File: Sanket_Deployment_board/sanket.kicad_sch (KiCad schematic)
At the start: 38 parts, among them J1 Conn_01x03, J2 Conn_02x03_Counter_Clockwise, J3 Conn_02x03_Counter_Clockwise, J4 Conn_01x01_Socket, J7 Conn_01x01_Socket, J8 Conn_01x05, Q1 NMOS, Q2 NMOS, U2 SN74LVC1G17QDCKRQ1, U3 TPS5420D, U4 74AHC1G00

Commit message: Routing done, 1st review to be done
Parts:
- removed J7: Conn_01x01_Socket, Connector_PinSocket_2.54mm:PinSocket_1x01_P2.54mm_Vertical, symbol Connector:Conn_01x01_Socket
- removed Q1, Q2: NMOS, NMOS_sanket:LFPAK56_SOT669_NEX-M, symbol Simulation_SPICE:NMOS
- removed TP3, TP4: TestPoint, TestPoint:TestPoint_THTPad_1.0x1.0mm_Drill0.5mm, symbol Connector:TestPoint
- removed U4: 74AHC1G00, NAND_sanket:DCK5_TEX-L, symbol 74xGxx:74AHC1G00
- added MOSFET1, MOSFET2: BUK9Y21-40E_115, NMOS_sanket:LFPAK56_SOT669_NEX-M, symbol NMOS_ADS:BUK9Y21-40E_115
- added U1: SN74LV1T00DCKR, NAND_sanket:DCK5_TEX-L, symbol NAND_ADS:SN74LV1T00DCKR
- C1: value 2u2 -> (none)
- C10: value 4.7u -> (none)
- C2, C8: value 100n -> (none)
- C3: value 10n -> (none)
- C4, C5: value 47u -> (none)
- C6: value 150p -> (none)
- C9: value 1800p -> (none)
- D1: value D -> (none); footprint Wurth inductor:DIOM7959X261N -> Diode_in_TP5420:CR_MBRS340_ONS-M
- H1, H2, H3, H4: value MountingHole -> (none)
- J1: value Conn_01x03 -> (none)
- J4: value Conn_01x01_Socket -> (none)
- J8: value Conn_01x05 -> (none)
- L1: value 18u -> (none)
- R1: value 1k -> (none)
- R2, R3, R4: value 100k -> (none)
- R5: value 1M -> (none)
- R6: value 549 -> (none)
- R7: value 5.9K -> (none)
- R8: value 10k -> (none)
- TP1, TP2: value TestPoint -> (none)
- U2: value SN74LVC1G17QDCKRQ1 -> (none); footprint Package_TO_SOT_SMD:SOT-353_SC-70-5 -> Schmitt_trigger_ADS:DCK5-M
- U3: value TPS5420D -> (none); footprint Package_SO:SOIC-8_3.9x4.9mm_P1.27mm -> TPS5420:D8-M
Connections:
- net 3V3: now also J2.6 (Pin_6), U1.5 (VCC); no longer J2.1 (Pin_1)
- net ARM: now also MOSFET1.4
- net BurnWire1IN: now also J2.1 (Pin_1); no longer J2.4 (Pin_4)
- net BurnWire1OUT: now also J2.2 (Pin_2), J2.4 (Pin_4), J3.1 (Pin_1); no longer J2.5 (Pin_5), J2.6 (Pin_6), J3.4 (Pin_4)
- net DEPLOY: now also U1.4 (Y)
- net DeployerDetectionSW1OUT: now also J2.5 (Pin_5), J3.6 (Pin_6); no longer J2.2 (Pin_2), J3.1 (Pin_1)
- net DeployerDetectionSW2OUT: now also J3.5 (Pin_5); no longer J3.2 (Pin_2)
- net FIRE: now also MOSFET2.4, U1.2 (B)
- net GND: now also MOSFET2.1, MOSFET2.2, MOSFET2.3, U1.3 (GND); no longer J3.5 (Pin_5), J3.6 (Pin_6)
- net TriggerOUT: now also U1.1 (A)
- new net: MOSFET1.1, MOSFET1.2, MOSFET1.3, MOSFET2.5
- new net NMOS_DRAIN: J3.2 (Pin_2), J3.4 (Pin_4), MOSFET1.5
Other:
- moved on the sheet: J2, R3, R4

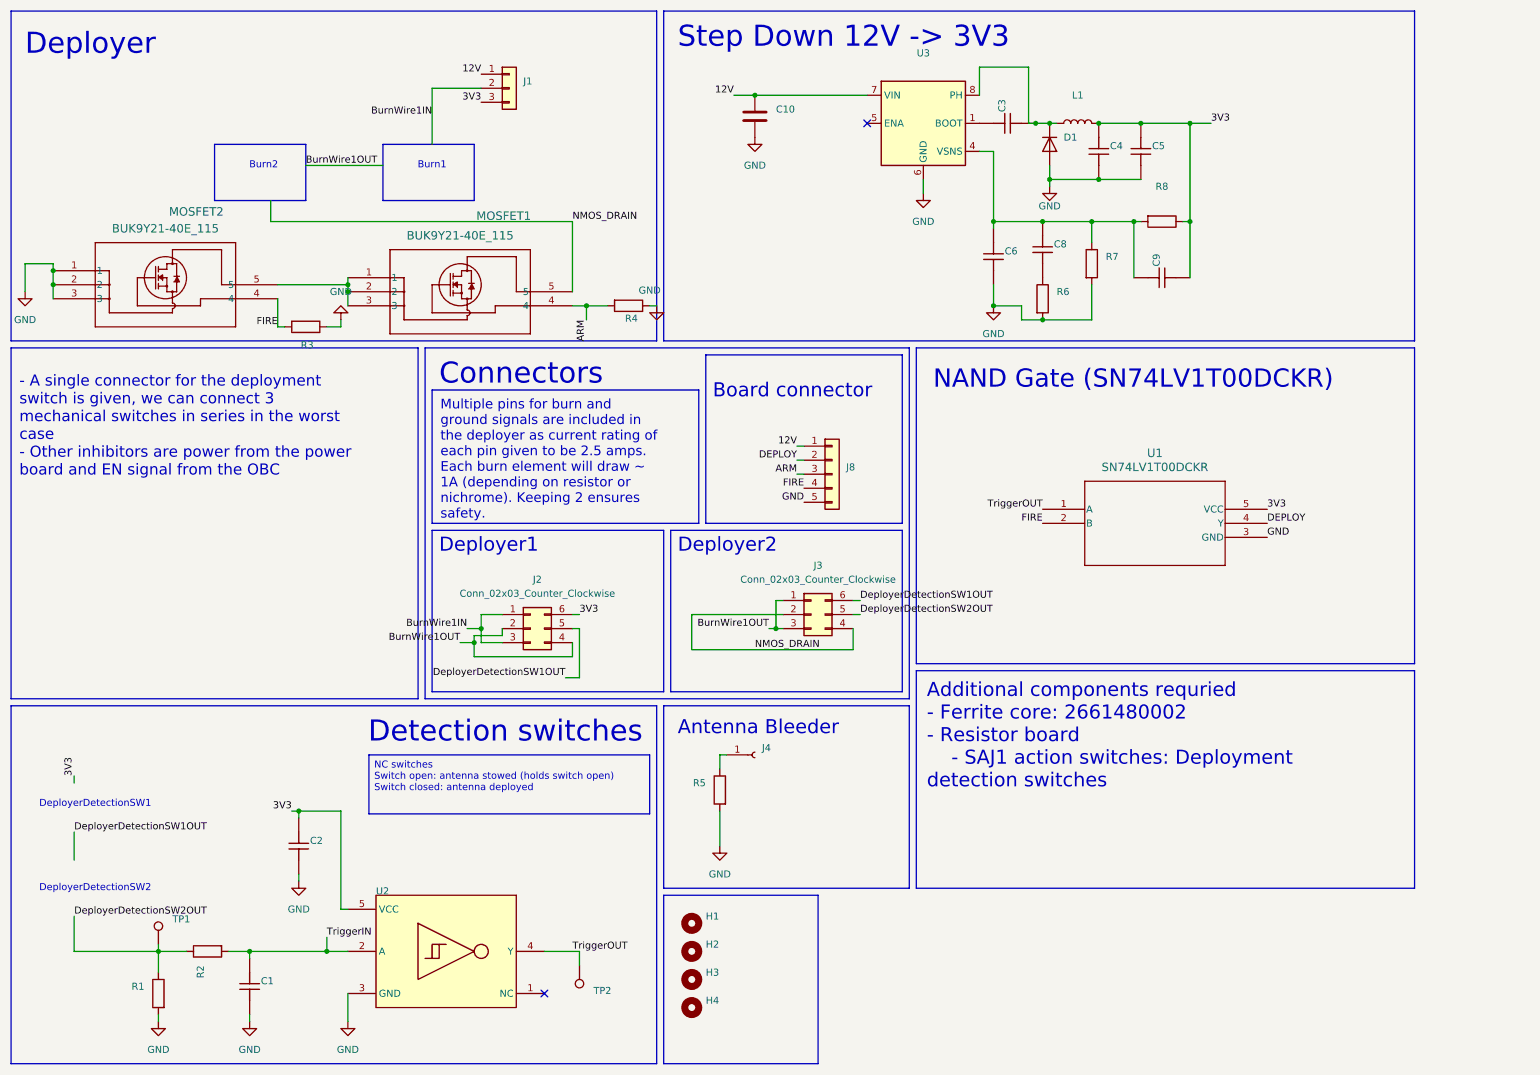
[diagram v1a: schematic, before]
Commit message: Added missing holw in resistor board, removed NAND gate, added more testpoints
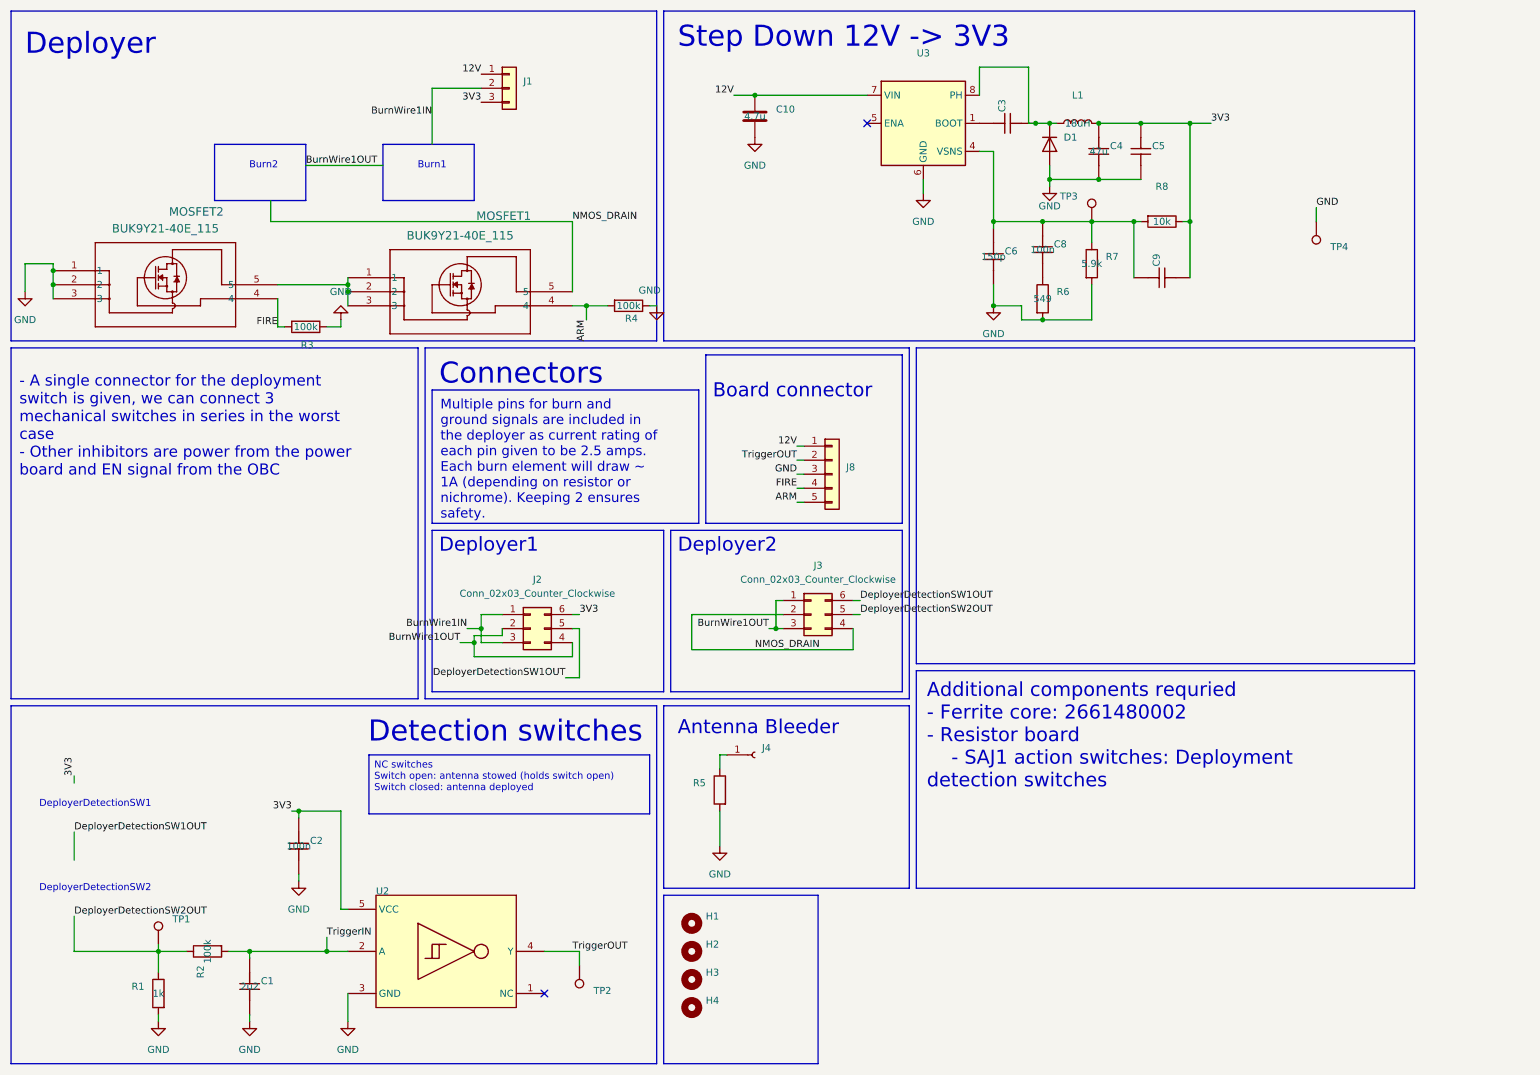
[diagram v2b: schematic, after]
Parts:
- removed U1: SN74LV1T00DCKR, NAND_sanket:DCK5_TEX-L, symbol NAND_ADS:SN74LV1T00DCKR
- added TP3, TP4: (no value), TestPoint:TestPoint_THTPad_1.0x1.0mm_Drill0.5mm, symbol Connector:TestPoint
- C1: value (none) -> 2u2
- C10: value (none) -> 4.7u
- C2, C8: value (none) -> 100n
- C4, C5: value (none) -> 47u
- C6: value (none) -> 150p
- L1: value (none) -> 18uH
- R1: value (none) -> 1k
- R2, R3, R4: value (none) -> 100k
- R6: value (none) -> 549
- R7: value (none) -> 5.9k
- R8: value (none) -> 10k
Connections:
- net DEPLOY is gone; now on net TriggerOUT: J8.2 (Pin_2)
- net ARM: now also J8.5 (Pin_5); no longer J8.3 (Pin_3)
- net GND: now also J8.3 (Pin_3), TP4.1; no longer J8.5 (Pin_5)
- net at C6.2, C8.2, C9.2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: now also TP3.1
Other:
- note removed: "NAND Gate (SN74LV1T00DCKR)"

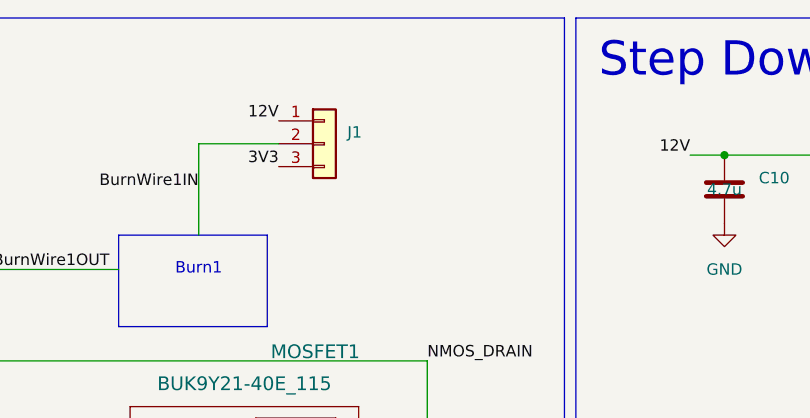
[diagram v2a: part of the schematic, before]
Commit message: Added extra pads for sized resistors
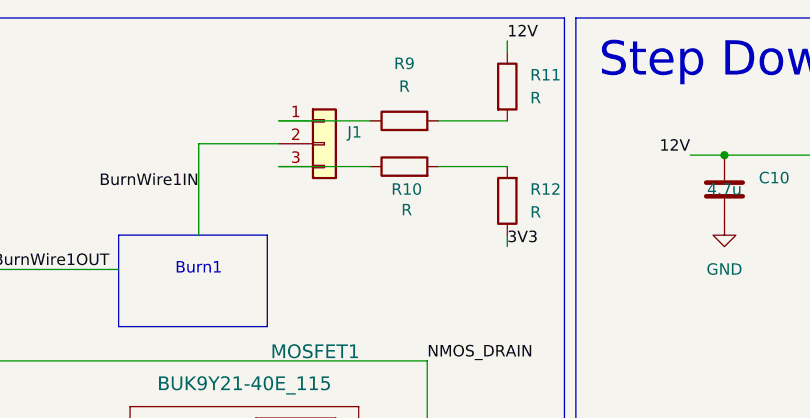
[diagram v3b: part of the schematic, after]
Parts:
- added R10, R11, R12, R9: R, Resistor_SMD:R_0805_2012Metric, symbol Device:R
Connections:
- net 12V: now also R11.1; no longer J1.1 (Pin_1)
- net 3V3: now also R12.1; no longer J1.3 (Pin_3)
- new net: R10.2, R12.2
- new net: J1.3 (Pin_3), R10.1
- new net: J1.1 (Pin_1), R9.1
- new net: R11.2, R9.2

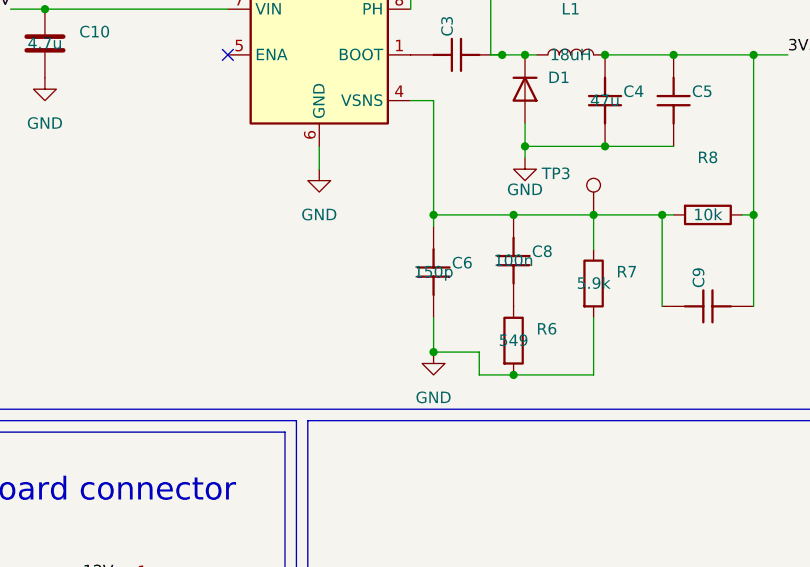
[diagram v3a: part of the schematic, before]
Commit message: Resistor board for nichrome added
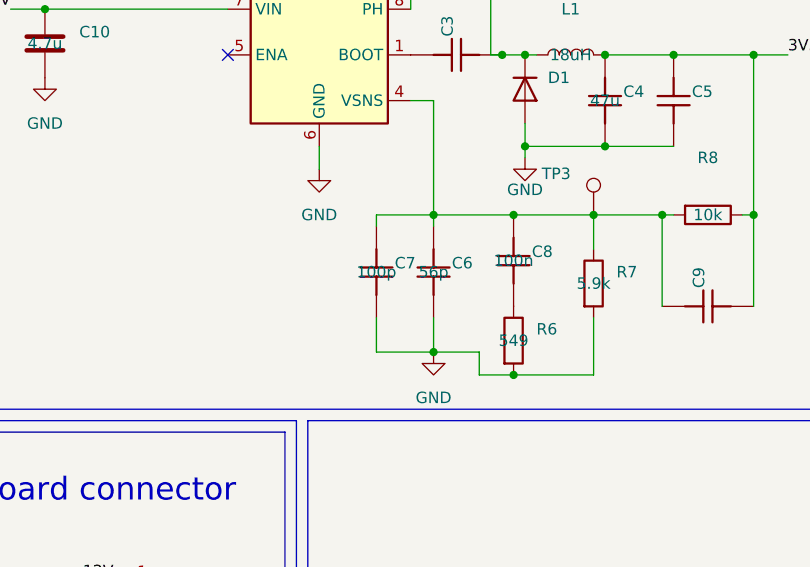
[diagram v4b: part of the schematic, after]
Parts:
- added C7: 100p, Capacitor_SMD:C_0805_2012Metric, symbol sanket 4.0-altium-import:root_1_CAP-CER-0.1u-16V
- C6: value 150p -> 56p
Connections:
- net GND: now also C7.1
- net at C6.2, C8.2, C9.2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: now also C7.2

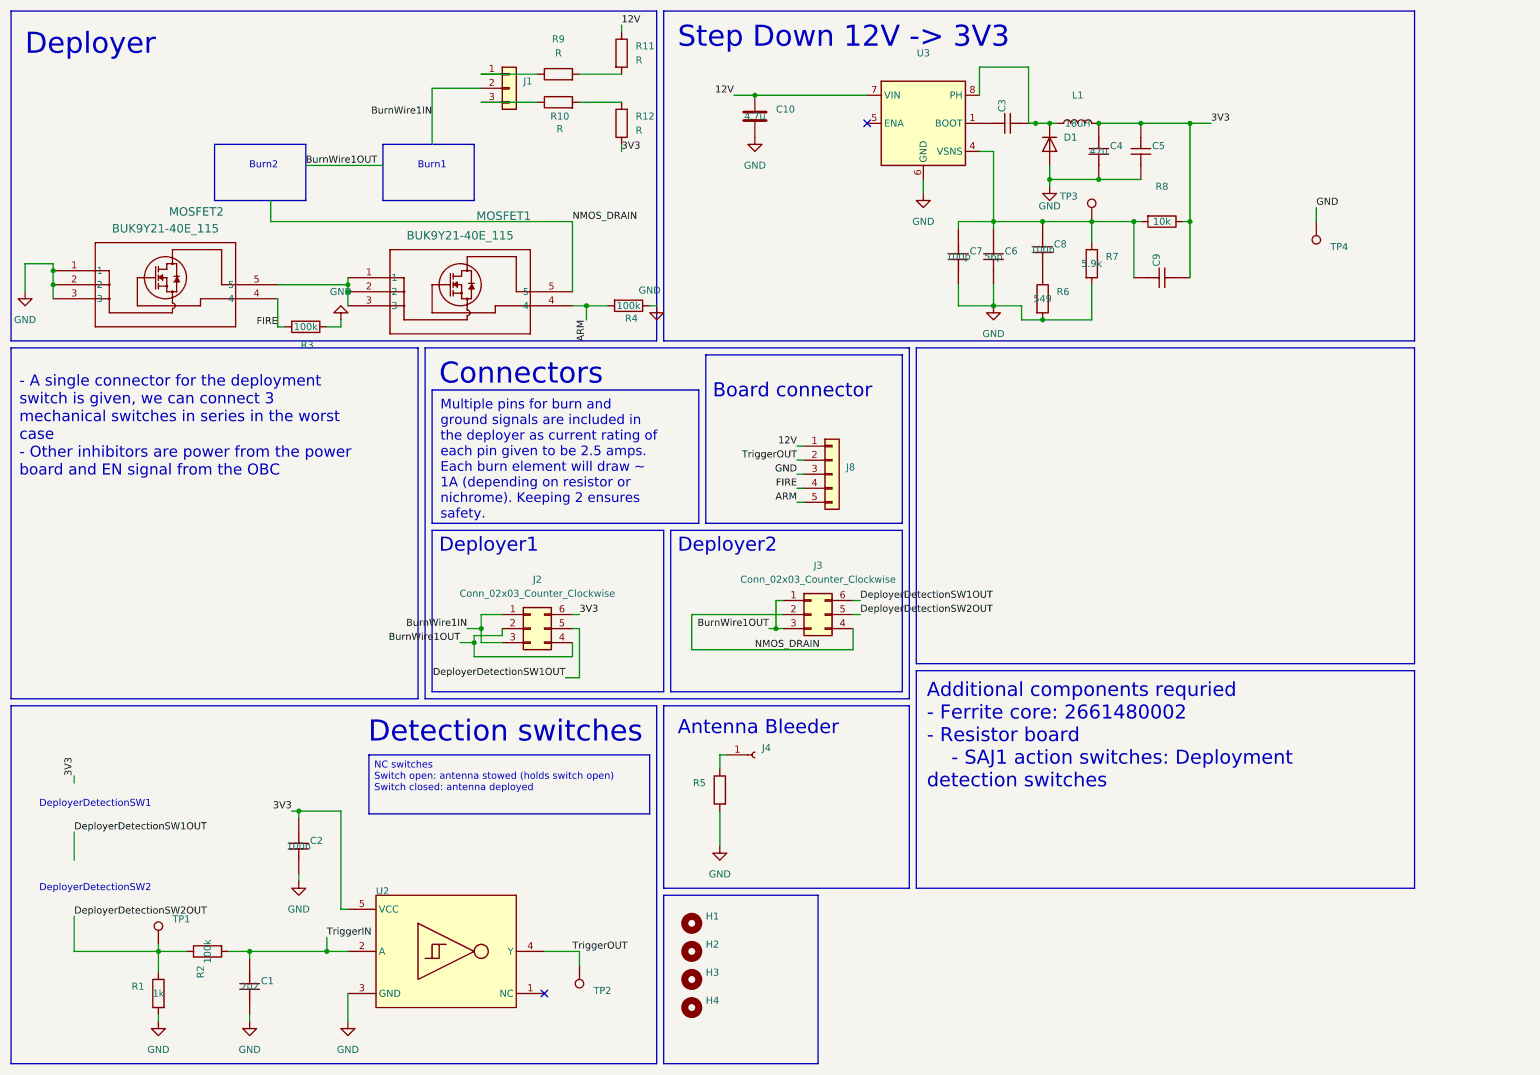
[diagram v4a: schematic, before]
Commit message: Added antenna bleeder, switched FIRE and ARM with each other, Corrected Schmitt trigger symbol to non-inverting
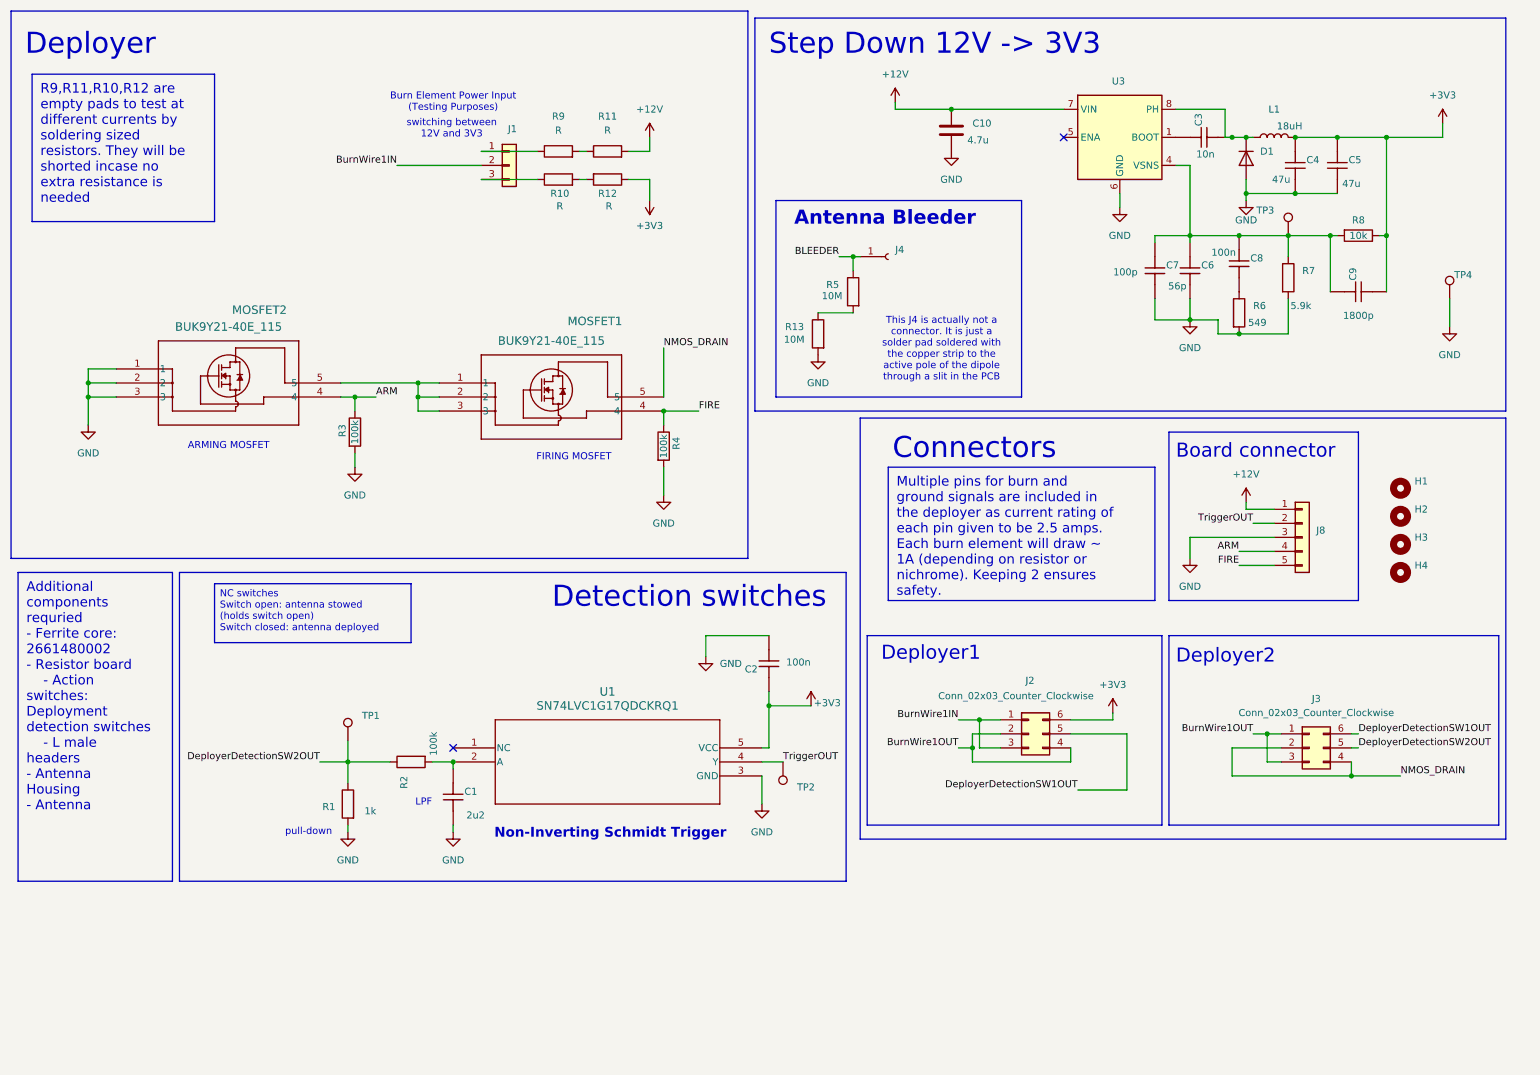
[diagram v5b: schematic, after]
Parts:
- removed U2: (no value), Schmitt_trigger_ADS:DCK5-M, symbol sanket 4.0-altium-import:root_0_IC-SN74LVC1G14QDCKRQ1
- added R13: 10M, Resistor_SMD:R_0805_2012Metric, symbol Device:R
- added U1: SN74LVC1G17QDCKRQ1, Schmitt_trigger_ADS:DCK5-M, symbol Schmitt_trigger_ADS:SN74LVC1G17QDCKRQ1
- C3: value (none) -> 10n
- C9: value (none) -> 1800p
- J4: footprint Connector_PinSocket_2.54mm:PinSocket_1x01_P2.54mm_Vertical -> Connector_Wire:SolderWirePad_1x01_SMD_3x6mm
- R5: value (none) -> 10M
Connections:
- net ARM: now also J8.4 (Pin_4), MOSFET2.4, R3.1; no longer J8.5 (Pin_5), MOSFET1.4, R4.2
- net FIRE: now also J8.5 (Pin_5), MOSFET1.4, R4.1; no longer J8.4 (Pin_4), MOSFET2.4, R3.2
- net GND: now also R3.2, R4.2, R13.2, U1.3 (GND); no longer R3.1, R4.1, R5.2
- net TriggerOUT: now also U1.4 (Y)
- net BLEEDER: now reaches J4.1 (Pin_1), R5.1
- net at R9.2: now also R11.1; no longer R11.2
- net 12V renamed +12V
- net +12V: now also R11.2; no longer R11.1
- net 3V3 renamed +3V3
- net +3V3: now also U1.5 (VCC)
- net TriggerIN: no longer names the net of C1.2, R2.2
- net TriggerIN: now also U1.2 (A)
- new net: R13.1, R5.2
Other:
- note added: "ARMING MOSFET"
- note added: "Burn Element Power Input (Testing Purposes)"
- note added: "FIRING MOSFET"
- note added: "LPF"
- note added: "Non-Inverting Schmidt Trigger"
- note added: "This J4 is actually not a connector. It is just a solder pad soldered with the copper strip to the active pole of the dipole through a slit in the PCB"
- note added: "pull-down"
- note added: "switching between 12V and 3V3"
- note removed: "Burn1"
- note removed: "Burn2"
- note removed: "DeployerDetectionSW1"
- note removed: "DeployerDetectionSW2"
- company: Student Satellite Program -> IIT Bombay Student Satellite Program
- moved on the sheet: C1, C10, C2, C3, C4, C5, C6, C7, C8, C9, D1, H1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
